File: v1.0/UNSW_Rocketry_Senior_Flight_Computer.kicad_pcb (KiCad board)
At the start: 4 copper layers, 60 x 60 mm, 132 parts, among them J1 BATT_XT60, J2 Micro_SD_Card_Det1, J3 USB_C_Receptacle_USB2.0_16P, J4 SWD, J5 Conn_01x04, J6 PYRO_XT60, J7 J_PYRO1, J8 J_PYRO2, Q1 DMG2301L, Q2 AO3401A, Q3 AO3400A, Q4 AO3400A, Q5 AO3400A, U1 STM32L452RETx, U10 PC817, U11 PC817, U2 TPS63060, U3 SPX3819M5-L-3-3, U4 H3LIS331DL, U5 MS5611 #1, U6 LIS3DH, U7 MS5611 #2, U8 USBLC6-2SC6, U9 PC817, Y1 8MHz

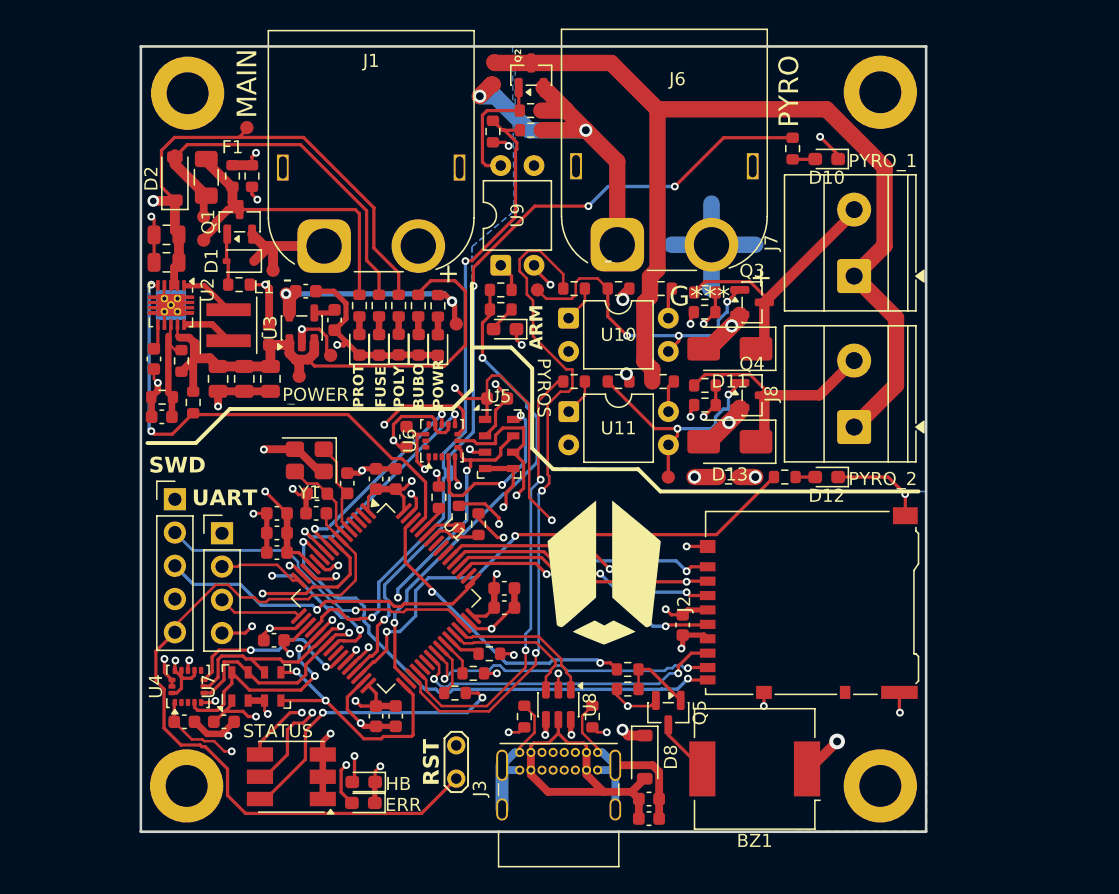
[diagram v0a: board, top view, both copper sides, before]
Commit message: v1.0: update schematics and PCB layout
Co-Authored-By: Claude Opus 4.7 (1M context) <noreply@anthropic.com>
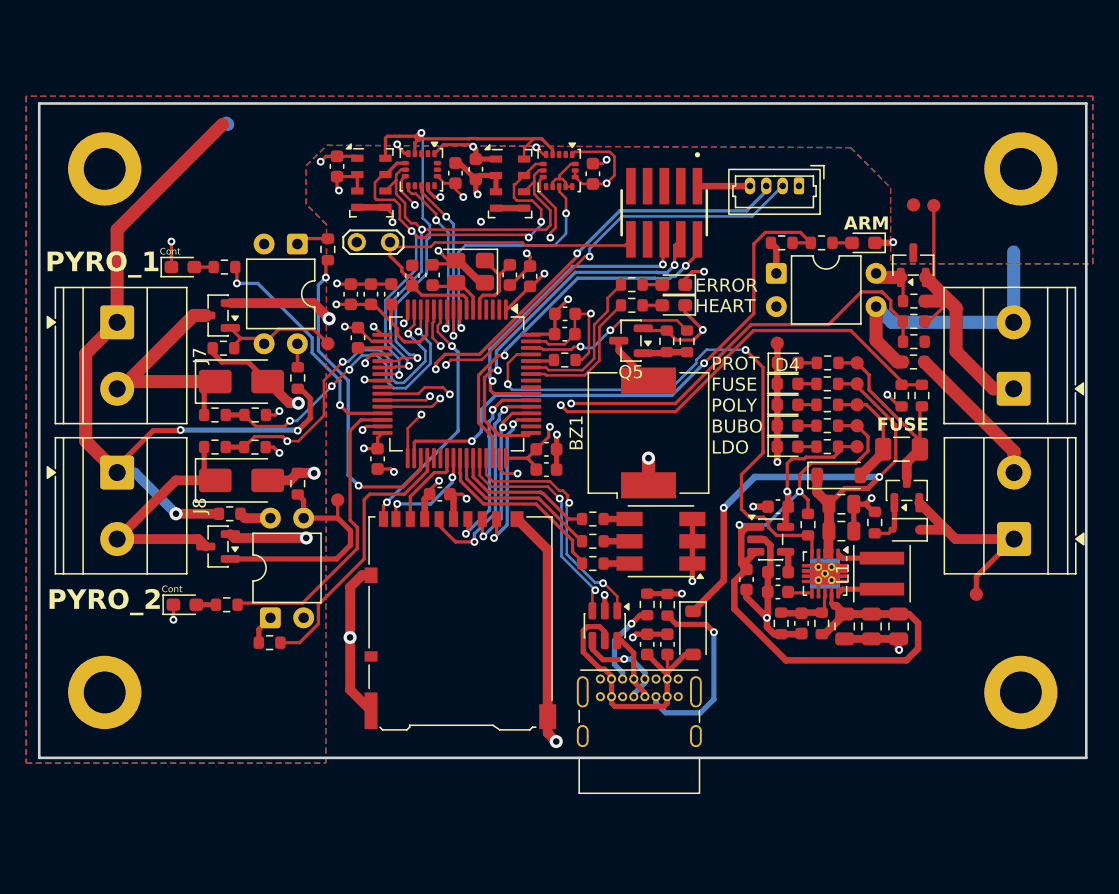
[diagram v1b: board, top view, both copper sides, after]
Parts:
- removed G***: LOGO, UNSW_ROCKETRY_LIBRARY:ROCKETRY_LOGO_LARGE
- removed G***: LOGO, UNSW_ROCKETRY_LIBRARY:ROCKETRY_LOGO_SMALL
- removed G***: ImageLogo, UNSW_ROCKETRY_LIBRARY:JUNO_LARGE_0.15
- removed J4: SWD, Connector_PinHeader_2.54mm:PinHeader_1x05_P2.54mm_Vertical
- removed J6: PYRO_XT60, Connector_AMASS:AMASS_XT60PW-M_1x02_P7.20mm_Horizontal
- added J10: J_BATT, TerminalBlock_Phoenix:TerminalBlock_Phoenix_MKDS-1,5-2-5.08_1x02_P5.08mm_Horizontal, F.Cu at (187.1, 107.4)
- added J9: J_PYRO_BAT, TerminalBlock_Phoenix:TerminalBlock_Phoenix_MKDS-1,5-2-5.08_1x02_P5.08mm_Horizontal, F.Cu at (187.1, 96.0)
- J1: value BATT_XT60 -> SWD; footprint Connector_AMASS:AMASS_XT60PW-M_1x02_P7.20mm_Horizontal -> UNSW_ROCKETRY_LIBRARY:SAMTEC_FTSH-105-01-X-DV-K-X
- J5: footprint Connector_PinHeader_2.54mm:PinHeader_1x04_P2.54mm_Vertical -> Connector_Molex:Molex_PicoBlade_53047-0410_1x04_P1.25mm_Vertical
- moved H4 64.1 mm to (187.6, 119.2)
- moved H3 59.7 mm to (117.6, 119.2)
- moved TP1 59.2 mm to (184.2, 111.7)
- moved F1 57.0 mm to (178.5, 100.6), turned to 0 degrees
- moved J7 56.4 mm to (118.5, 90.9), turned to -90 degrees
- moved J8 56.4 mm to (118.5, 102.3), turned to -90 degrees
- moved C14 56.3 mm to (173.9, 106.8), turned to 180 degrees
- moved D2 55.6 mm to (173.7, 102.6), turned to 0 degrees
- moved R7 55.3 mm to (180.0, 96.5)
- moved Q1 55.0 mm to (178.9, 103.7)
- moved D1 54.9 mm to (178.8, 106.7)
- moved C15 54.8 mm to (173.9, 104.8), turned to 0 degrees
- moved U2 54.0 mm to (172.6, 110.1)
- moved L1 53.4 mm to (177.0, 110.1)
- moved R2 52.9 mm to (172.4, 113.9)
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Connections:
- U1 pad 55: unconnected-(U1-PB3-Pad55) -> SWO
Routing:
- net VBAT_FUSED: track 129.6 -> 43.1 mm
- net PYRO1_CONT_LED: track 63.7 -> 18.3 mm, vias 4 -> 2
- net +3.3V: track 108.6 -> 73.4 mm, vias 16 -> 12
- net UART_RX: track 6.39 -> 39.0 mm, vias 0 -> 3
- net UART_TX: track 6.42 -> 38.4 mm, vias 0 -> 3
- net Net-(D15-A): track 31.4 -> 1.50 mm, vias 2 -> 0
- net NRST: track 58.4 -> 28.6 mm
- net Net-(D14-BA): track 30.6 -> 1.97 mm, vias 2 -> 0
- net PYRO1_GATE: track 52.3 -> 25.0 mm
- net Net-(D14-GA): track 28.7 -> 1.97 mm, vias 2 -> 0
- net Net-(D16-A): track 27.2 -> 1.50 mm, vias 2 -> 0
- net SWO: track 0.00 -> 24.4 mm, vias 0 -> 2
- net PYRO_GND: track 26.6 -> 48.1 mm, vias 5 -> 4
- net Net-(D14-RA): track 22.9 -> 1.97 mm, vias 2 -> 0
- net SD_CD: track 40.1 -> 19.2 mm
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- added copper zone on In2.Cu, net +3.3V
- added copper zone on F.Cu, net PYRO_BATT
- removed copper zone on B.Cu, net +3.3V
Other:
- board size 60 x 60 mm -> 80 x 50 mm
- board text added: "Cont"
- board text added: "ERROR"
- board text added: "HEART"
- board text added: "LDO"
- board text removed: "30Km ALT 400g ACL Dual Pyro 1s 2s Input"
- board text removed: "DASHIELL RUSSELL"
- board text removed: "ERR"
- board text removed: "HB"
- board text removed: "MAIN"
- board text removed: "POWER"
- board text removed: "POWR"
- board text removed: "PYRO"
- board text removed: "PYROS"
- board text removed: "RST"
- board text removed: "STATUS"
- board text removed: "SWD"
- board text removed: "UART"
- board text removed: "UNSW ROCKETRY SENIOR FLIGHT COMPUTER"
